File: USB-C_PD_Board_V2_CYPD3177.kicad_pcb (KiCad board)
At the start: 2 copper layers, 43 parts, among them J1 Conn_01x03, J2 Type-C_6P, J3 I2C, J4 Conn_01x03, Q1 DMP3098LSD, SW1 SW_SPDT, SW2 SW_SPDT, U1 CYPD3177-24LQ

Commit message: started routing
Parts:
- added G***: LOGO, LOGO, B.Cu at (149.1, 91.8)
- added H1: MountingHole, MountingHole:MountingHole_3.2mm_M3_DIN965_Pad, F.Cu at (138.0, 85.0)
- added H2: MountingHole, MountingHole:MountingHole_3.2mm_M3_DIN965_Pad, F.Cu at (121.0, 98.0)
- D1, TP1, TP2, TP3: moved to B.Cu
- moved J1 62.3 mm to (170.2, 89.0), turned to 180 degrees
- moved J4 60.9 mm to (170.2, 94.0), turned to 0 degrees
- moved C3 58.2 mm to (164.8, 86.5), turned to 180 degrees
- moved R8 56.1 mm to (162.4, 91.5)
- moved C7 55.4 mm to (152.7, 92.9), turned to -90 degrees
- moved C6 54.2 mm to (150.6, 92.9), turned to -90 degrees
- moved D1 53.6 mm to (125.4, 100.2), turned to 0 degrees
- moved R2 53.3 mm to (129.3, 100.5), turned to 0 degrees
- moved C5 50.5 mm to (148.5, 93.0), turned to -90 degrees
- moved R10 48.4 mm to (151.9, 95.9)
- moved U1 47.9 mm to (142.0, 90.7)
- moved C1 47.1 mm to (134.7, 92.4)
- moved R1 47.1 mm to (137.4, 92.0)
- moved R7 47.0 mm to (158.2, 91.5)
- moved C9 46.0 mm to (126.2, 83.8), turned to -90 degrees
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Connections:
- R18 pad 1: Net-(SW2-C) -> Net-(R18-Pad1)
- R4 pad 1: VDD -> +3V3
- R5 pad 1: VDD -> +3V3
- SW2 pad 1: Net-(SW2-A) -> unconnected-(SW2-A-Pad1)
- SW4 pad 1: Net-(R17-Pad1) -> Net-(R18-Pad1)
- SW4 pad 2: Net-(R16-Pad1) -> Net-(R17-Pad1)
- SW4 pad 3: Net-(SW2-A) -> Net-(SW2-C)
- SW4 pad 4: Net-(SW2-A) -> Net-(SW2-C)
- SW4 pad 5: Net-(R15-Pad1) -> Net-(R16-Pad1)
- SW4 pad 6: unconnected-(SW4-Pad6) -> Net-(R15-Pad1)
- U1 pad 2: Net-(SW2-B) -> Net-(SW1-B)
- U1 pad 5: Net-(SW1-B) -> Net-(SW2-B)
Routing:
- net Net-(R14-Pad1): track 0.00 -> 15.0 mm, vias 0 -> 1
- net +3V3: track 0.00 -> 14.3 mm
- net Net-(R18-Pad1): track 0.00 -> 13.8 mm, vias 0 -> 1
- net Net-(SW2-B): track 0.00 -> 13.2 mm, vias 0 -> 1
- net Net-(R12-Pad1): track 0.00 -> 13.2 mm
- net Net-(R13-Pad1): track 0.00 -> 12.0 mm
- net Net-(R16-Pad1): track 0.00 -> 11.2 mm
- net VBUS: track 0.00 -> 11.0 mm
- net GND: track 0.00 -> 10.9 mm, vias 0 -> 52
- net Net-(R17-Pad1): track 0.00 -> 10.6 mm
- net Net-(J2-CC2): track 0.00 -> 10.4 mm
- net Net-(SW1-B): track 0.00 -> 10.2 mm, vias 0 -> 1
- net Net-(D1-A): track 0.00 -> 9.92 mm, vias 0 -> 1
- net Net-(J2-CC1): track 0.00 -> 9.74 mm, vias 0 -> 2
- net Net-(R11-Pad1): track 0.00 -> 9.20 mm
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- added copper zone on F.Cu, net +VSW
- added copper zone on In2.Cu, net +VSW
- added copper zone on B.Cu, net GND
- added copper zone on F.Cu, net GND
- added copper zone on In1.Cu, net GND
- added copper zone on F.Cu, net Net-(D1-A)
- added copper zone on F.Cu, net VBUS
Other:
- board outline added: 55 x 25 mm
- copper layers 2 -> 4
- board text added: "1"
- board text added: "12"
- board text added: "15V"
- board text added: "2"
- board text added: "20V"
- board text added: "3"
- board text added: "4A"
- board text added: "5"
- board text added: "5A"
- board text added: "9"
- board text added: "<--"
- board text added: "Potpurri USB-C PD Board using CYPD3177 Version 2.0"
- board text added: "|"

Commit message: routing
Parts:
- moved TP1 19.1 mm to (157.5, 90.6)
- moved TP2 9.76 mm to (142.0, 85.3)
- moved TP3 9.75 mm to (144.1, 85.3)
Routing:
- net +3V3: track 14.3 -> 55.5 mm, vias 0 -> 1
- net Net-(J2-CC1): track 9.74 -> 29.9 mm, vias 2 -> 3
- net Net-(J3-Pin_1): track 0.00 -> 19.7 mm, vias 0 -> 2
- net Net-(D1-A): track 9.92 -> 27.0 mm, vias 1 -> 2
- net Net-(J2-CC2): track 10.4 -> 24.6 mm
- net Net-(U1-SAFE_PWR_EN): track 0.00 -> 13.5 mm, vias 0 -> 1
- net Net-(J3-Pin_2): track 0.00 -> 11.0 mm
- net Net-(U1-VBUS_MIN): track 0.00 -> 9.00 mm
- net Net-(U1-ISNK_FINE): track 0.00 -> 8.16 mm
- net Net-(U1-FAULT): track 0.00 -> 7.43 mm, vias 0 -> 1
- net Net-(U1-VCCD): track 0.00 -> 5.71 mm, vias 0 -> 2
- net Net-(D1-K): track 8.44 -> 13.9 mm
- net Net-(U1-FLIP): track 0.00 -> 3.73 mm, vias 0 -> 1
- net Net-(D2-A): track 0.00 -> 2.65 mm
- net +VSW: track 1.42 -> 2.05 mm
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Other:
- board text added: "15 V"
- board text added: "4 A"
- board text added: "Potpurri USB-C PD Board using CYPD3177, Version 2.0"
- board text removed: "15V"
- board text removed: "4A"
- board text removed: "Potpurri USB-C PD Board using CYPD3177 Version 2.0"

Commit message: pcb layout and routing done!
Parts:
- moved R10 5.19 mm to (146.7, 96.0), turned to -90 degrees
- moved C5 2.36 mm to (148.9, 95.3)
- moved C6 2.29 mm to (151.1, 95.1)
- moved C7 2.26 mm to (153.0, 95.1)
- moved C10 2.14 mm to (143.6, 94.9), turned to 180 degrees
- moved TP1 1.75 mm to (156.9, 92.2)
- moved R6 1.22 mm to (146.6, 87.1)
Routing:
- net Net-(U1-VBUS_FET_EN): track 0.00 -> 33.4 mm, vias 0 -> 2
- net Net-(SW1-B): track 10.2 -> 29.9 mm
- net Net-(SW2-B): track 13.2 -> 29.6 mm, vias 1 -> 2
- net Net-(SW2-C): track 0.00 -> 12.9 mm
- net Net-(SW1-A): track 0.00 -> 12.6 mm
- net +3V3: track 55.5 -> 47.8 mm, vias 1 -> 3
- net GND: track 11.0 -> 18.3 mm, vias 62 -> 67
- net Net-(U1-VBUS_MIN): track 9.00 -> 5.37 mm
- net Net-(U1-VCCD): track 5.71 -> 2.75 mm, vias 2 -> 0
- net Net-(U1-FLIP): track 3.73 -> 4.94 mm
- net Net-(U1-ISNK_FINE): track 8.16 -> 7.34 mm
- net Net-(U1-FAULT): track 7.43 -> 8.14 mm
- net Net-(R14-Pad1): track 15.0 -> 15.6 mm

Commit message: Donegit add .
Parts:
- added G***: LOGO, LOGO, F.Cu at (146.3, 90.7)
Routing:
- net GND: vias 67 -> 74
- added copper zone on B.Cu, net +VSW

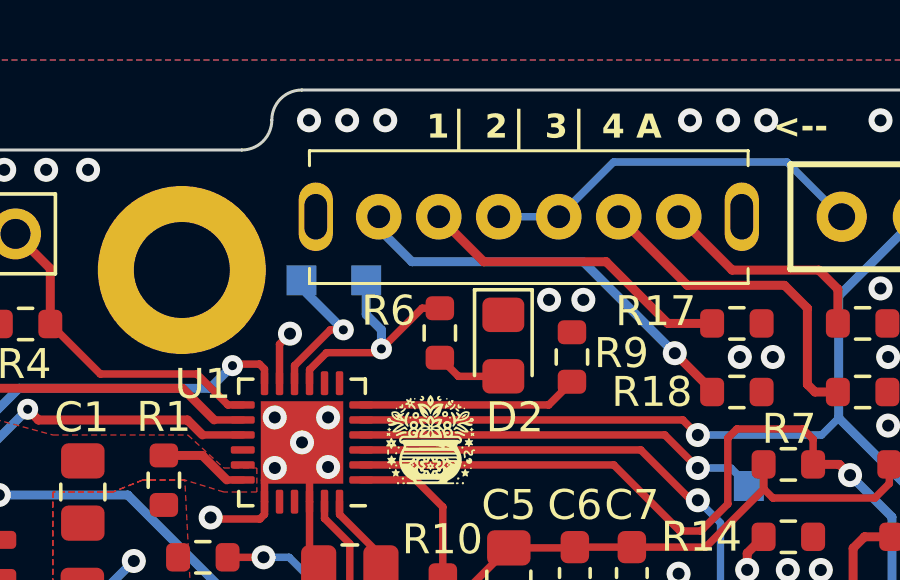
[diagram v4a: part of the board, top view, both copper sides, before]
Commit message: Added jlc serial number silk screen
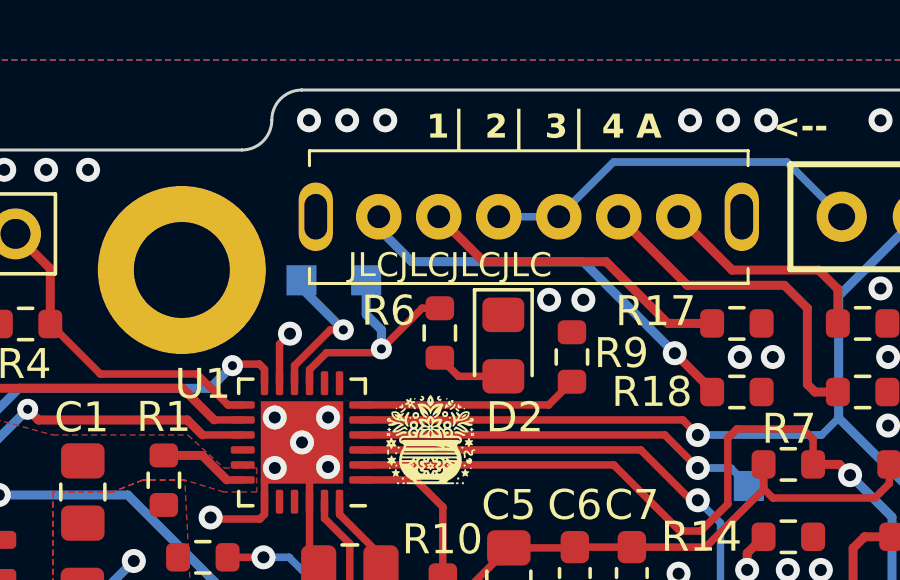
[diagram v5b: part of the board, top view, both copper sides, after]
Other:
- board text added: "JLCJLCJLCJLC"
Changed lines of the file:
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@@
     (effects (font (size 0.8 0.8) (thickness 0.15) bold) (justify left bottom))
+  )
+  (gr_text "JLCJLCJLCJLC" (at 146.939 84.836) (layer "F.SilkS")
+    (effects (font (size 0.8 0.8) (thickness 0.1)))
   )
   (gr_text "|" (at 149 80.795) (layer "F.SilkS")

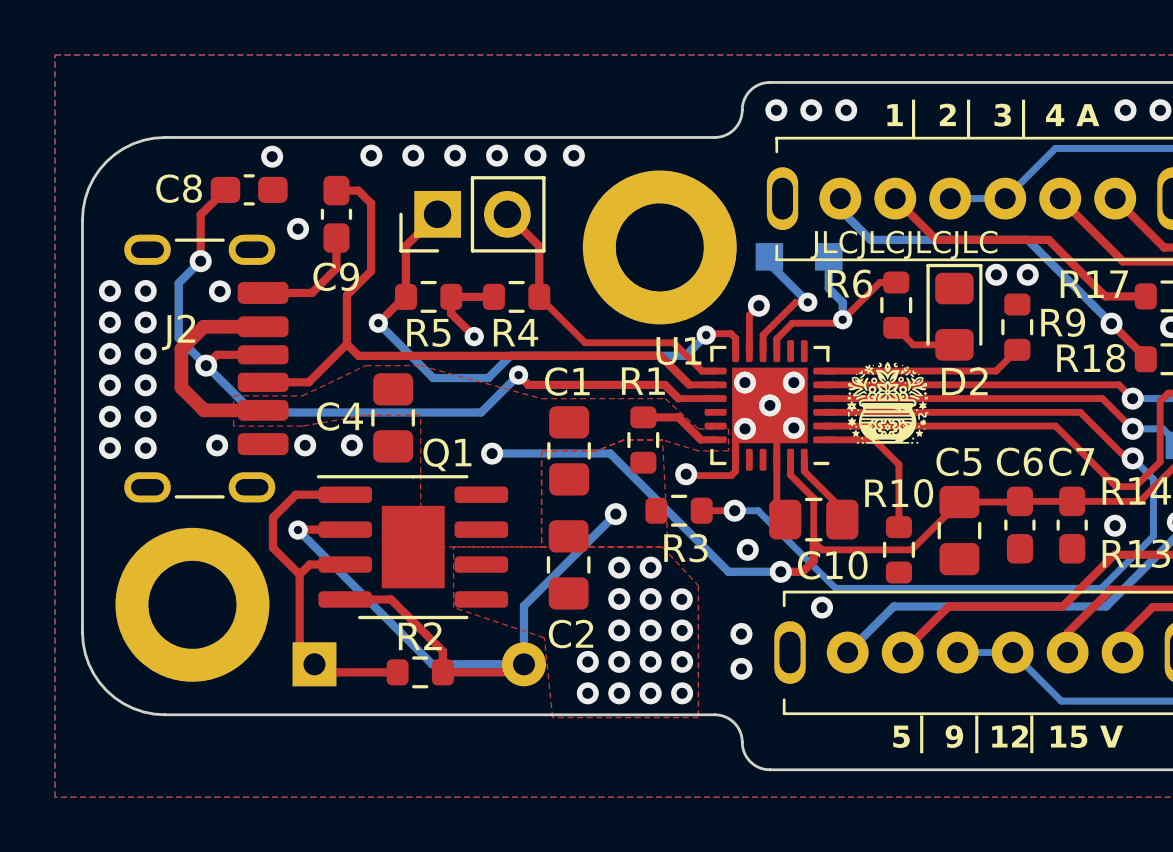
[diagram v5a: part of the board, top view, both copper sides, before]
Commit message: added turn on/off switch, added diode to indicate on state
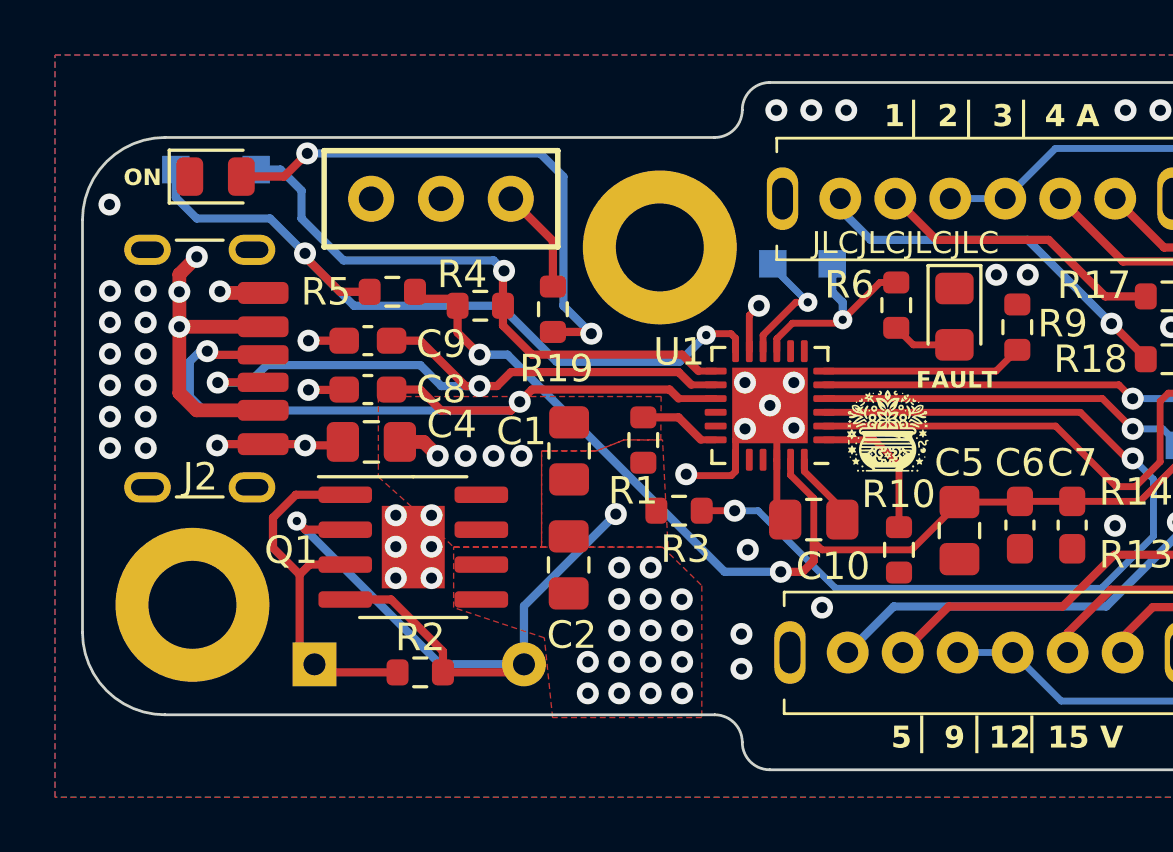
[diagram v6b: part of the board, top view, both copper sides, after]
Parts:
- removed J3: I2C, Connector_PinHeader_2.54mm:PinHeader_1x02_P2.54mm_Vertical
- added D3: LED, LED_SMD:LED_0805_2012Metric, F.Cu at (121.8, 82.4)
- added R19: 1k, Resistor_SMD:R_0603_1608Metric, F.Cu at (134.1, 87.2)
- added SW5: SW_SPDT, SS12D00_switch:Schiebeschalter SS-12D00, F.Cu at (130.0, 83.2)
- added TP4: TestPoint, TestPoint:TestPoint_Pad_1.0x1.0mm, B.Cu at (120.4, 82.2)
- added TP5: TestPoint, TestPoint:TestPoint_Pad_1.0x1.0mm, B.Cu at (123.3, 82.2)
- moved C8 8.45 mm to (127.4, 90.2), turned to 180 degrees
- moved C9 4.74 mm to (127.4, 88.4), turned to 180 degrees
- moved R4 1.36 mm to (131.5, 87.1)
- moved R5 1.33 mm to (128.3, 86.6)
- moved C4 1.18 mm to (127.5, 92.1), turned to 180 degrees
- moved G*** 1.02 mm to (146.3, 91.7)
- moved TP2 0.28 mm to (142.1, 85.6)
- moved TP3 0.28 mm to (144.3, 85.6)
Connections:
- J2 pad A9: VBUS -> Net-(SW5-A)
- J2 pad B9: VBUS -> Net-(SW5-A)
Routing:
- net Net-(D3-A): track 0.00 -> 20.0 mm, vias 0 -> 2
- net Net-(SW5-A): track 0.00 -> 11.6 mm, vias 0 -> 3
- net Net-(U1-HPI_SCL): track 11.0 -> 21.6 mm, vias 0 -> 1
- net Net-(U1-HPI_SDA): track 19.9 -> 27.9 mm
- net GND: track 18.3 -> 23.0 mm
- net VBUS: track 11.0 -> 8.38 mm, vias 0 -> 4
- net +3V3: track 47.8 -> 45.7 mm, vias 3 -> 2
- net Net-(J2-CC1): track 29.9 -> 29.0 mm, vias 3 -> 2
- net Net-(J2-CC2): vias 0 -> 2
- added copper zone on In2.Cu, net Net-(SW5-A)
- added copper zone on In2.Cu, net VBUS
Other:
- board text added: "FAULT"
- board text added: "ON"
- board text added: "Potpurri USB-C PD Board using CYPD3177, Version 2.1"
- board text added: "SCL"
- board text added: "SDA"
- board text removed: "Potpurri USB-C PD Board using CYPD3177, Version 2.0"

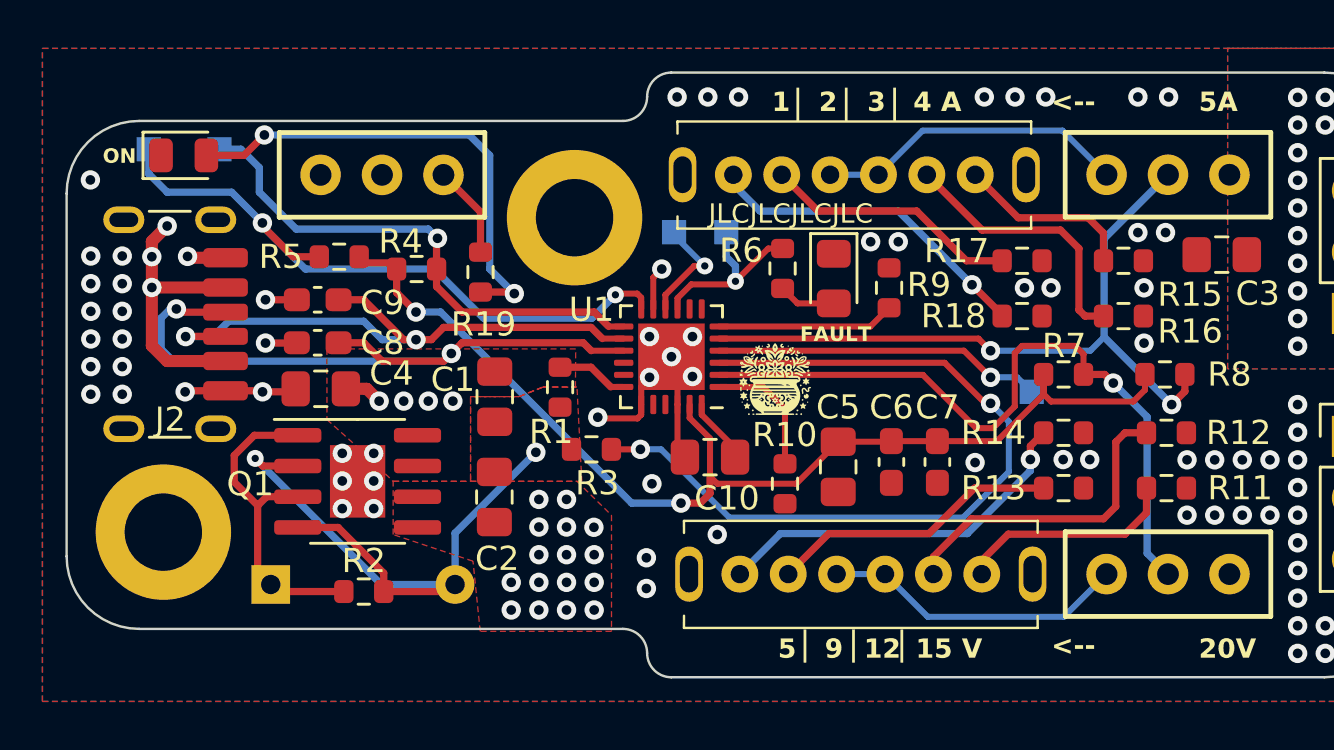
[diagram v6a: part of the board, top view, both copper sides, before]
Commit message: added tear drops and curved traces
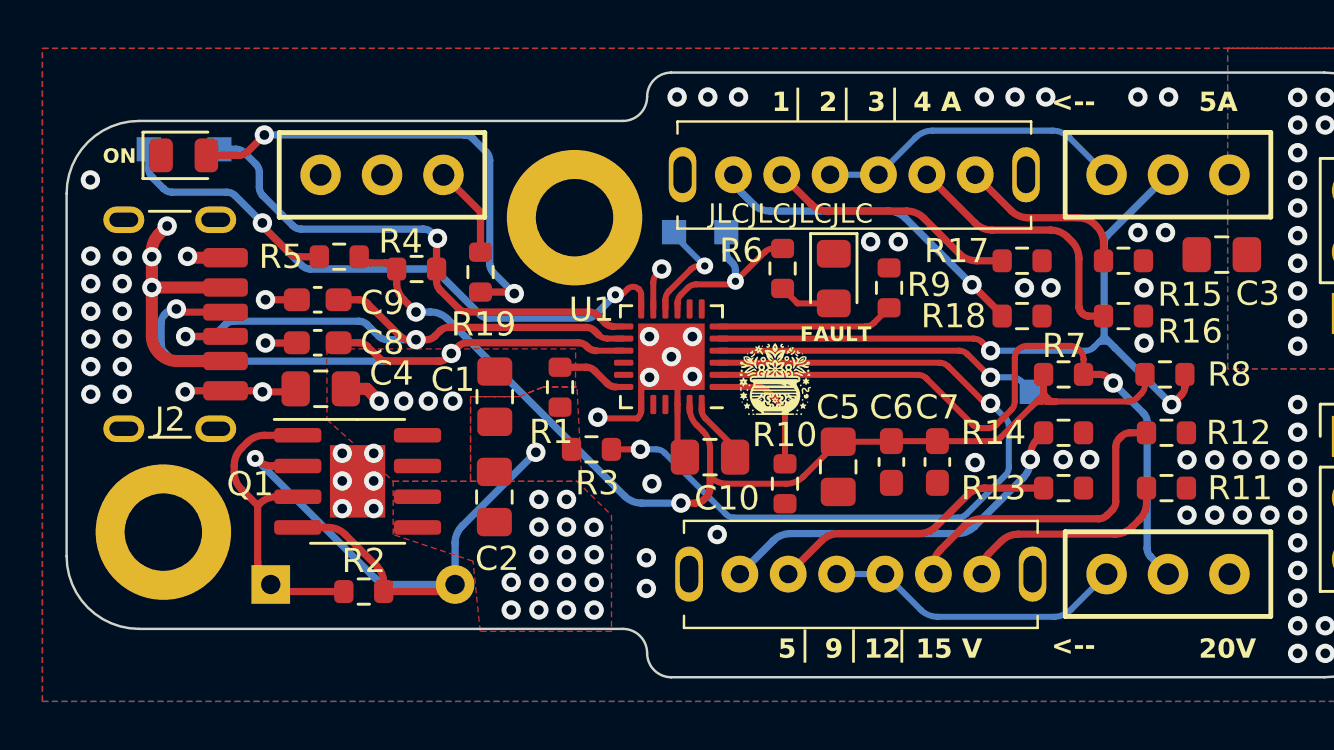
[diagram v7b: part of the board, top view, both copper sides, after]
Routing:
- net +3V3: track 45.7 -> 46.9 mm
- net Net-(SW2-B): track 29.6 -> 30.2 mm
